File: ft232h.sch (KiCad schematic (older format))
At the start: 14 parts, among them U1 93LCxxB, U4 FT232H, Y1 Crystal

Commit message: a bunch of stuff I guess. mostly layout.
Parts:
- C17, C21: footprint (none) -> Capacitors_SMD:C_0603
- C18: renamed from C20; footprint (none) -> Capacitors_SMD:C_0603
- C19: renamed from C16; footprint (none) -> Capacitors_SMD:C_0603
- C20: renamed from C18; footprint (none) -> Capacitors_SMD:C_0603
- C22: renamed from C19; footprint (none) -> Capacitors_SMD:C_0603
- L3, L4: footprint (none) -> Inductors_SMD:L_0603
- R14, R15, R16: footprint (none) -> Resistors_SMD:R_0603
- U3: renamed from U1; footprint (none) -> Housings_SOIC:SOIC-8_3.9x4.9mm_Pitch1.27mm
- U4: footprint (none) -> Housings_QFP:LQFP-48_7x7mm_Pitch0.5mm
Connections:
- net GND: now also C18.2; no longer C18.1
- net at L3.1, U4.3 (VPHY): now also C21.2; no longer C22.1
- net at U4.37 (VCCA): now also C18.1; no longer C18.2
- net at L4.1, U4.8 (VPLL): now also C22.1; no longer C21.2
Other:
- moved on the sheet: C17, C18, C21, C22, L3, L4, R14, U3

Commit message: pcb updates or something
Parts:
- removed Y1: Crystal, symbol Device:Crystal
- added Y1: Crystal_GND24, Crystals:Crystal_SMD_3225-4pin_3.2x2.5mm, symbol Device:Crystal_GND24
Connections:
- net GND: now also Y1.2, Y1.4
- net at C19.1, U4.1 (XCSI): now also Y1.1
- net at C20.1, U4.2 (XCSO): now also Y1.3
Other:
- moved on the sheet: C19, C20

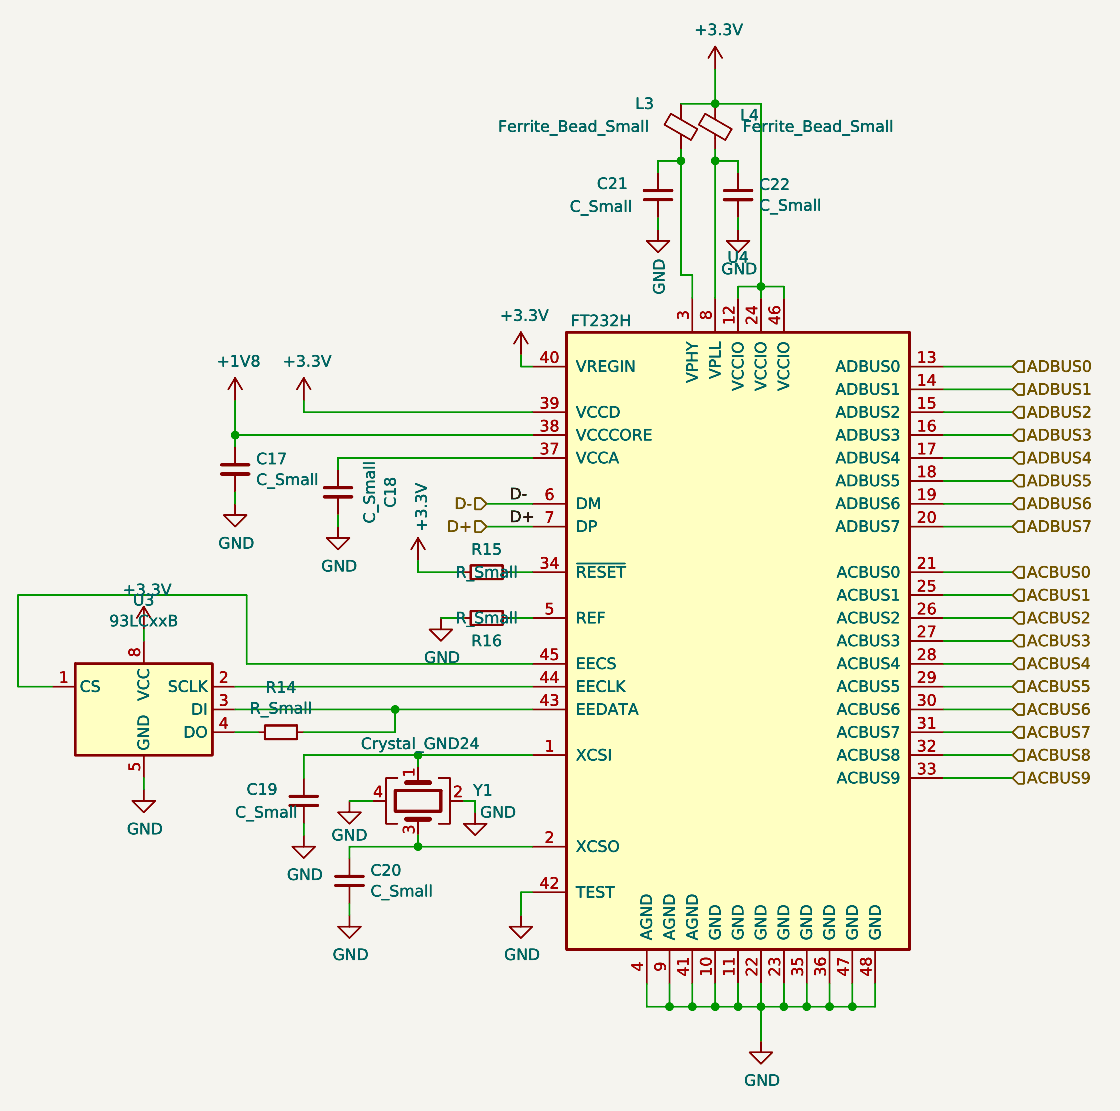
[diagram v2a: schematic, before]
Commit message: redirected 3D models for custom footprints on PCB
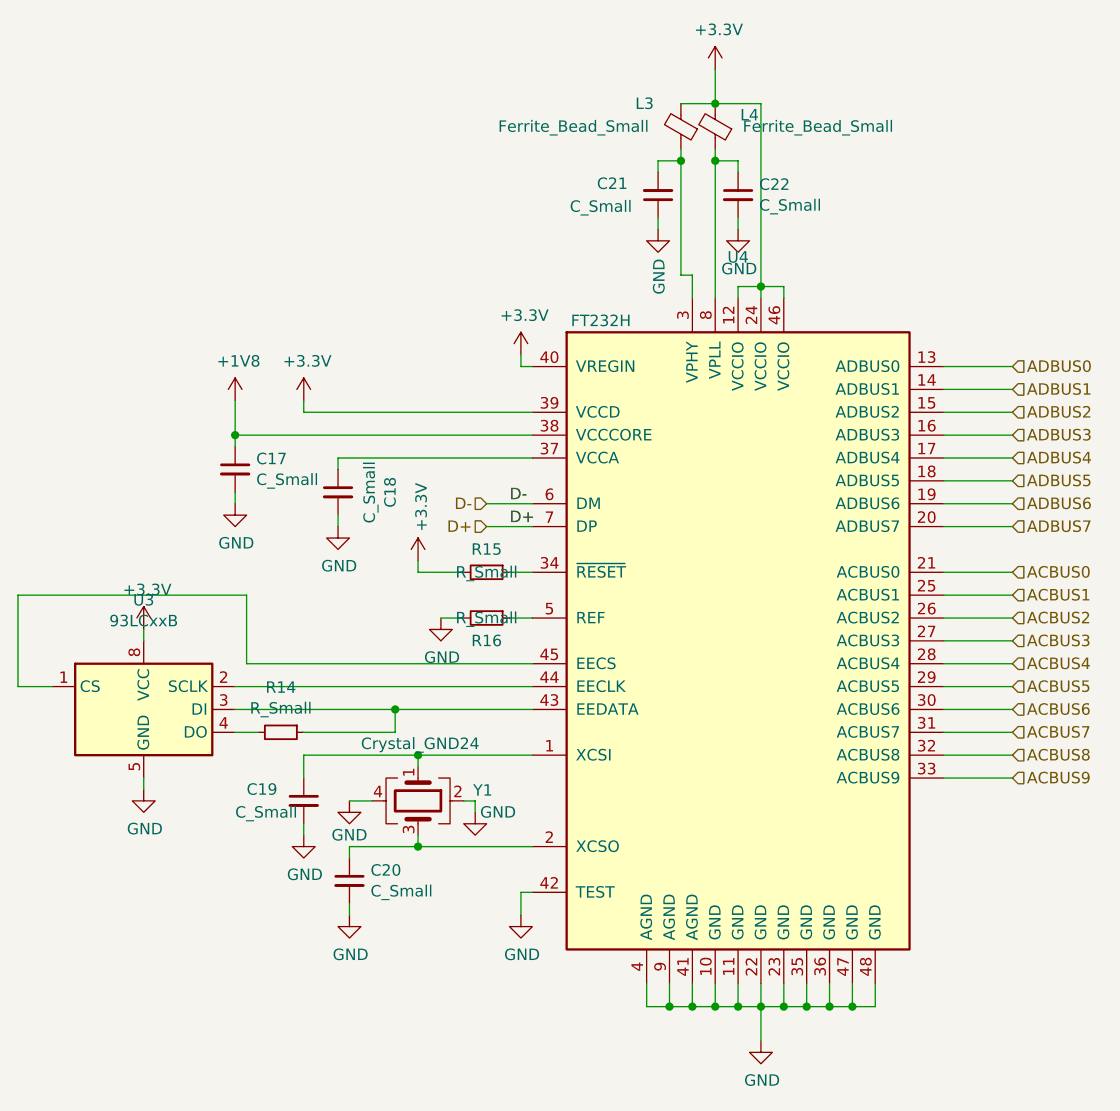
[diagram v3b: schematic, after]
